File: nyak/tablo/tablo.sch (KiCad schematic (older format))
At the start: 109 parts

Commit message: more wiring
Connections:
- net Earth: now also U?.4 (E1), U?.4 (E1), U?.5 (E2), U?.5 (E2), U?.8 (GND), U?.8 (GND), U?.9 (GND), UOD1.7 (GND), UOD2.7 (GND)
- net GPIO12: now reaches U?.11 (Load)
- net GPIO12: now also JRPI.32 (Pin_32)
- net C1: now reaches U?.2 (D0)
- net C1: now also JRPI.7 (Pin_7), U?.2 (D0), U?.2 (D0), U?.2 (D0), U?.2 (D0), U?.2 (D0)
- net VCC: now reaches U?.20 (VCC)
- net VCC: now also U?.16 (VCC), U?.16 (VCC), U?.20 (VCC), U?.20 (VCC), U?.20 (VCC), U?.20 (VCC), U?.20 (VCC), UOD1.14 (VCC), UOD2.14 (VCC)
- net C2: now reaches U?.3 (D1)
- net C2: now also JRPI.29 (Pin_29), U?.3 (D1), U?.3 (D1), U?.3 (D1), U?.3 (D1), U?.3 (D1)
- net C3: now reaches U?.4 (D2)
- net C3: now also JRPI.31 (Pin_31), U?.4 (D2), U?.4 (D2), U?.4 (D2), U?.4 (D2), U?.4 (D2)
- net C4: now reaches U?.5 (D3)
- net C4: now also JRPI.26 (Pin_26), U?.5 (D3), U?.5 (D3), U?.5 (D3), U?.5 (D3), U?.5 (D3)
- net C5: now reaches U?.6 (D4)
- net C5: now also JRPI.24 (Pin_24), U?.6 (D4), U?.6 (D4), U?.6 (D4), U?.6 (D4), U?.6 (D4)
- net C6: now reaches U?.7 (D5)
- net C6: now also JRPI.21 (Pin_21), U?.7 (D5), U?.7 (D5), U?.7 (D5), U?.7 (D5), U?.7 (D5)
- net C7: now reaches U?.8 (D6)
- net C7: now also JRPI.19 (Pin_19), U?.8 (D6), U?.8 (D6), U?.8 (D6), U?.8 (D6), U?.8 (D6)
- net C8: now reaches U?.9 (D7)
- net C8: now also JRPI.23 (Pin_23), U?.9 (D7), U?.9 (D7), U?.9 (D7), U?.9 (D7), U?.9 (D7)
- net GPIO13: now reaches U?.11 (Load)
- net GPIO13: now also JRPI.33 (Pin_33)
- net GPIO14: now reaches U?.11 (Load)
- net GPIO14: now also JRPI.8 (Pin_8)
- net GPIO15: now reaches U?.11 (Load)
- net GPIO15: now also JRPI.10 (Pin_10)
- net GPIO16: now reaches U?.11 (Load)
- net GPIO16: now also JRPI.36 (Pin_36)
- net GPIO17: now reaches U?.11 (Load)
- net GPIO17: now also JRPI.11 (Pin_11)
- net AR1: now reaches U?.1 (A0)
- net AR1: now also JRPI.12 (Pin_12), U?.1 (A0)
- net AR2: now reaches U?.2 (A1)
- net AR2: now also JRPI.35 (Pin_35), U?.2 (A1)
- net AR3: now reaches U?.3 (A2)
- net AR3: now also JRPI.38 (Pin_38), U?.3 (A2)
- net GPIO22: now reaches U?.6 (E3)
- net GPIO22: now also JRPI.15 (Pin_15)
- net GPIO21: now reaches U?.6 (E3)
- net GPIO21: now also JRPI.40 (Pin_40)

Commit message: footprints added
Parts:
- JC1: footprint (none) -> Connector_PinHeader_2.54mm:PinHeader_1x08_P2.54mm_Vertical
- JC2, JC3, JC4, JC5, JC6, JR1, JR2: renamed from JC?; footprint (none) -> Connector_PinHeader_2.54mm:PinHeader_1x08_P2.54mm_Vertical
- JRPI1: renamed from JRPI; footprint (none) -> Connector_PinSocket_2.54mm:PinSocket_2x20_P2.54mm_Vertical
- QR1, QR10, QR11, QR12, QR2, QR3, QR4, QR5, QR6, QR7, QR8, QR9: renamed from Q?; footprint (none) -> Package_TO_SOT_THT:TO-220-3_Vertical
- RC1, RC10, RC11, RC12, RC13, RC14, RC15, RC16, RC17, RC18, RC19, RC2, RC20, RC21, RC22, RC23, RC24, RC25, RC26, RC27, RC28, RC29, RC3, RC30, RC31, RC32, RC33, RC34, RC35, RC36, RC37, RC38, RC39, RC4, RC40, RC41, RC42, RC43, RC44, RC45, RC46, RC47, RC48, RC5, RC6, RC7, RC8, RC9, RRB1, RRB10, RRB11, RRB12, RRB2, RRB3, RRB4, RRB5, RRB6, RRB7, RRB8, RRB9, RRE1, RRE10, RRE11, RRE12, RRE2, RRE3, RRE4, RRE5, RRE6, RRE7, RRE8, RRE9: renamed from R?; footprint (none) -> Resistor_THT:R_Axial_DIN0204_L3.6mm_D1.6mm_P7.62mm_Horizontal
- UC1, UC2, UC3, UC4, UC5, UC6: renamed from U?; footprint (none) -> Package_DIP:DIP-18_W7.62mm
- UDM1, UDM2: renamed from U?; footprint (none) -> Package_DIP:DIP-16_W7.62mm
- UL1, UL2, UL3, UL4, UL5, UL6: renamed from U?; footprint (none) -> Package_DIP:DIP-20_W7.62mm
- UOD1, UOD2: footprint (none) -> Package_DIP:DIP-14_W7.62mm
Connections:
- net Earth: now also QR1.3 (E), QR10.3 (E), QR11.3 (E), QR12.3 (E), QR2.3 (E), QR3.3 (E), QR4.3 (E), QR5.3 (E), QR6.3 (E), QR7.3 (E), QR8.3 (E), QR9.3 (E), RRE1.1, RRE10.1, RRE11.1, RRE12.1, RRE2.1, RRE3.1, RRE4.1, RRE5.1, RRE6.1, RRE7.1, RRE8.1, RRE9.1
- net at UL1.1 (OE): now also JRPI1.16 (Pin_16), UL2.1 (OE), UL3.1 (OE), UL4.1 (OE), UL5.1 (OE), UL6.1 (OE)

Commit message: more tracks
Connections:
- net at QR7.1 (B), RRE7.2: now also RRB7.2; no longer RRB8.2
- net at QR8.1 (B), RRE8.2: now also RRB8.2; no longer RRB7.2
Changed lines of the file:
@@
 	550  2200 550  2150
 Wire Wire Line
-	3300 2600 3300 1850
-Wire Wire Line
-	3300 1850 3000 1850
-Wire Wire Line
 	3000 1850 3000 1900
-Connection ~ 3000 1850
 Wire Wire Line
 	3000 1850 2800 1850
@@
 	3300 2700 3250 2700
 Wire Wire Line
-	3250 2700 3250 1800
-Wire Wire Line
-	3250 1800 2550 1800
-Wire Wire Line
 	2350 1800 2350 1850
 Wire Wire Line
 	2550 1800 2550 1900
-Connection ~ 2550 1800
 Wire Wire Line
 	2550 1800 2350 1800
@@
 Wire Wire Line
 	2900 3900 2900 3700
-Wire Bus Line
-	7700 1100 7700 10400
 Connection ~ 2450 4000
 Connection ~ 2900 3700
@@
 Wire Wire Line
 	650  2600 1000 2600
+Wire Wire Line
+	3300 2600 3300 1800
+Wire Wire Line
+	3300 1800 2550 1800
+Connection ~ 2550 1800
+Wire Wire Line
+	3250 2700 3250 1850
+Wire Wire Line
+	3250 1850 3000 1850
+Wire Bus Line
+	7700 1100 7700 10400
+Connection ~ 3000 1850
 $EndSCHEMATC

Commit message: more pcb
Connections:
- net Earth: now also UL1.10 (GND)
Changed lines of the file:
@@
 EESchema Schematic File Version 4
-LIBS:tablo-cache
-EELAYER 26 0
+EELAYER 30 0
 EELAYER END
 $Descr A3 16535 11693
@@
 	8950 10300 9100 10300
 Wire Wire Line
-	8450 2250 9500 2250
-Wire Wire Line
 	9500 2250 9500 1950
-Wire Wire Line
-	8450 4000 9500 4000
-Wire Wire Line
-	9500 4000 9500 3650
 Wire Wire Line
 	8450 5700 9500 5700
@@
 Wire Wire Line
 	9700 3650 9500 3650
-Connection ~ 9500 3650
 Wire Wire Line
 	9500 3650 9500 3600
@@
 Wire Wire Line
 	3250 1850 3000 1850
+Connection ~ 3000 1850
+Connection ~ 9500 3650
+Wire Wire Line
+	9500 4000 9500 3650
+Wire Wire Line
+	8450 4000 9500 4000
+Wire Wire Line
+	9500 2250 8450 2250
+Wire Wire Line
+	8450 2250 8450 2300
 Wire Bus Line
 	7700 1100 7700 10400
-Connection ~ 3000 1850
 $EndSCHEMATC

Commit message: seems to be finished
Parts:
- added JTAP1: Conn_01x02_Male, Connector_PinHeader_2.54mm:PinHeader_1x02_P2.54mm_Vertical, symbol Connector:Conn_01x02_Male
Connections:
- net Earth: now also JRPI1.6 (Pin_6), JTAP1.2 (Pin_2)
- net VCC: now also JRPI1.2 (Pin_2), JTAP1.1 (Pin_1)
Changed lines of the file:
@@
 Wire Wire Line
 	8450 2250 8450 2300
+$Comp
+L Connector:Conn_01x02_Male JTAP1
+U 1 1 5DEAD8D0
+P 5400 7700
+F 0 "JTAP1" H 5508 7881 50  0000 C CNN
+F 1 "Conn_01x02_Male" H 5508 7790 50  0000 C CNN
+F 2 "Connector_PinHeader_2.54mm:PinHeader_1x02_P2.54mm_Vertical" H 5400 7700 50  0001 C CNN
+F 3 "~" H 5400 7700 50  0001 C CNN
+	1    5400 7700
+	1    0    0    -1
+$EndComp
+$Comp
+L power:Earth #PWR0121
+U 1 1 5DEADD9C
+P 5900 7900
+F 0 "#PWR0121" H 5900 7650 50  0001 C CNN
+F 1 "Earth" H 5900 7750 50  0001 C CNN
+F 2 "" H 5900 7900 50  0001 C CNN
+F 3 "~" H 5900 7900 50  0001 C CNN
+	1    5900 7900
+	1    0    0    -1
+$EndComp
+Wire Wire Line
+	5900 7900 5900 7800
+Wire Wire Line
+	5900 7800 5600 7800
+$Comp
+L power:VCC #PWR0122
+U 1 1 5DF5E14E
+P 5900 7600
+F 0 "#PWR0122" H 5900 7450 50  0001 C CNN
+F 1 "VCC" H 5917 7773 50  0000 C CNN
+F 2 "" H 5900 7600 50  0001 C CNN
+F 3 "" H 5900 7600 50  0001 C CNN
+	1    5900 7600
+	1    0    0    -1
+$EndComp
+Wire Wire Line
+	5600 7700 5900 7700
+Wire Wire Line
+	5900 7700 5900 7600
+$Comp
+L power:VCC #PWR0123
+U 1 1 5DFB5291
+P 6050 4600
+F 0 "#PWR0123" H 6050 4450 50  0001 C CNN
+F 1 "VCC" H 6067 4773 50  0000 C CNN
+F 2 "" H 6050 4600 50  0001 C CNN
+F 3 "" H 6050 4600 50  0001 C CNN
+	1    6050 4600
+	1    0    0    -1
+$EndComp
+Wire Wire Line
+	5850 4650 6050 4650
+Wire Wire Line
+	6050 4650 6050 4600
+$Comp
+L power:Earth #PWR0124
+U 1 1 5E00CD77
+P 6000 4750
+F 0 "#PWR0124" H 6000 4500 50  0001 C CNN
+F 1 "Earth" H 6000 4600 50  0001 C CNN
+F 2 "" H 6000 4750 50  0001 C CNN
+F 3 "~" H 6000 4750 50  0001 C CNN
+	1    6000 4750
+	-1   0    0    1
+$EndComp
+Wire Wire Line
+	5850 4850 6000 4850
+Wire Wire Line
+	6000 4850 6000 4750
 Wire Bus Line
 	7700 1100 7700 10400

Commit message: updated rpi gpio connector footprint
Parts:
- JRPI1: footprint Connector_PinSocket_2.54mm:PinSocket_2x20_P2.54mm_Vertical -> Connector_PinHeader_2.54mm:PinHeader_2x20_P2.54mm_Vertical
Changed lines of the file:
@@
 EESchema Schematic File Version 4
+LIBS:tablo-cache
 EELAYER 30 0
 EELAYER END
@@
 F 0 "JRPI1" H 5600 6667 50  0000 C CNN
 F 1 "Conn_02x20_Odd_Even" H 5600 6576 50  0000 C CNN
-F 2 "Connector_PinSocket_2.54mm:PinSocket_2x20_P2.54mm_Vertical" H 5550 5550 50  0001 C CNN
+F 2 "Connector_PinHeader_2.54mm:PinHeader_2x20_P2.54mm_Vertical" H 5550 5550 50  0001 C CNN
 F 3 "~" H 5550 5550 50  0001 C CNN
 	1    5550 5550

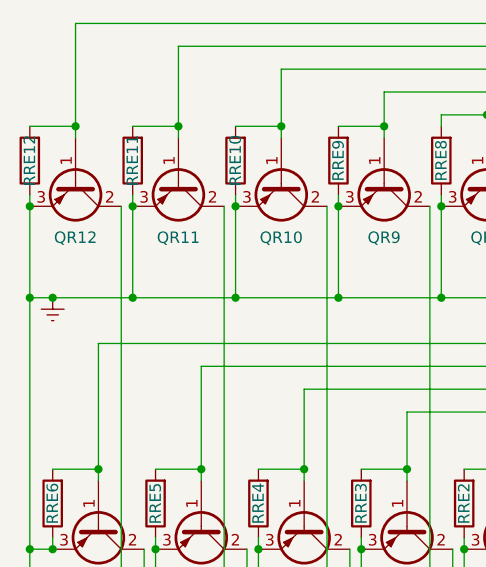
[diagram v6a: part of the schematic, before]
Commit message: Fixed row switch PNP transistor emitter connection from GND to VCC
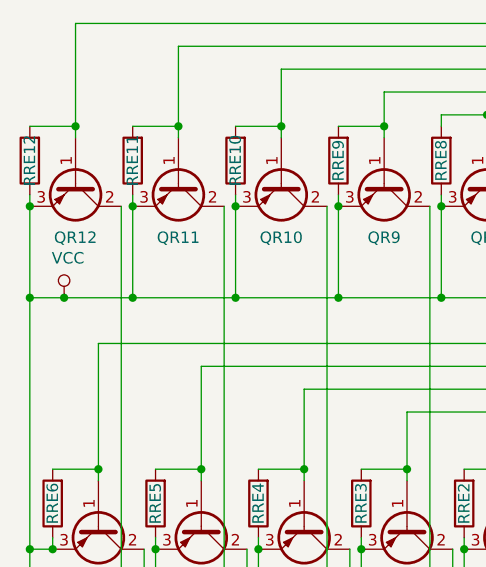
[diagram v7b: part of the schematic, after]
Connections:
- net Earth: no longer QR1.3 (E), QR10.3 (E), QR11.3 (E), QR12.3 (E), QR2.3 (E), QR3.3 (E), QR4.3 (E), QR5.3 (E), QR6.3 (E), QR7.3 (E), QR8.3 (E), QR9.3 (E), RRE1.1, RRE10.1, RRE11.1, RRE12.1, RRE2.1, RRE3.1, RRE4.1, RRE5.1, RRE6.1, RRE7.1, RRE8.1, RRE9.1
- net VCC: now also QR1.3 (E), QR10.3 (E), QR11.3 (E), QR12.3 (E), QR2.3 (E), QR3.3 (E), QR4.3 (E), QR5.3 (E), QR6.3 (E), QR7.3 (E), QR8.3 (E), QR9.3 (E), RRE1.1, RRE10.1, RRE11.1, RRE12.1, RRE2.1, RRE3.1, RRE4.1, RRE5.1, RRE6.1, RRE7.1, RRE8.1, RRE9.1
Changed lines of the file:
@@
 EESchema Schematic File Version 4
-LIBS:tablo-cache
 EELAYER 30 0
 EELAYER END
@@
 Title ""
 Date ""
-Rev ""
+Rev "1.1"
 Comp ""
 Comment1 ""
@@
 	550  2200 550  2600
 Wire Wire Line
-	550  2600 650  2600
-Wire Wire Line
 	1000 2600 1000 2200
 Connection ~ 550  2200
@@
 Connection ~ 2450 4000
 Connection ~ 2900 3700
-$Comp
-L power:Earth #PWR0120
-U 1 1 5F6E748E
-P 650 2600
-F 0 "#PWR0120" H 650 2350 50  0001 C CNN
-F 1 "Earth" H 650 2450 50  0001 C CNN
-F 2 "" H 650 2600 50  0001 C CNN
-F 3 "~" H 650 2600 50  0001 C CNN
-	1    650  2600
-	1    0    0    -1
-$EndComp
-Connection ~ 650  2600
-Wire Wire Line
-	650  2600 1000 2600
 Wire Wire Line
 	3300 2600 3300 1800
@@
 Wire Bus Line
 	7700 1100 7700 10400
+Wire Wire Line
+	550  2600 700  2600
+$Comp
+L power:VCC #PWR0120
+U 1 1 5E138797
+P 700 2600
+F 0 "#PWR0120" H 700 2450 50  0001 C CNN
+F 1 "VCC" H 717 2773 50  0000 C CNN
+F 2 "" H 700 2600 50  0001 C CNN
+F 3 "" H 700 2600 50  0001 C CNN
+	1    700  2600
+	1    0    0    -1
+$EndComp
+Connection ~ 700  2600
+Wire Wire Line
+	700  2600 1000 2600
 $EndSCHEMATC

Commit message: Updated resistor footprints to have 0.8mm holes instead of 0.7
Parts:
- RC1, RC10, RC11, RC12, RC13, RC14, RC15, RC16, RC17, RC18, RC19, RC2, RC20, RC21, RC22, RC23, RC24, RC25, RC26, RC27, RC28, RC29, RC3, RC30, RC31, RC32, RC33, RC34, RC35, RC36, RC37, RC38, RC39, RC4, RC40, RC41, RC42, RC43, RC44, RC45, RC46, RC47, RC48, RC5, RC6, RC7, RC8, RC9, RRB1, RRB10, RRB11, RRB12, RRB2, RRB3, RRB4, RRB5, RRB6, RRB7, RRB8, RRB9, RRE1, RRE10, RRE11, RRE12, RRE2, RRE3, RRE4, RRE5, RRE6, RRE7, RRE8, RRE9: footprint Resistor_THT:R_Axial_DIN0204_L3.6mm_D1.6mm_P7.62mm_Horizontal -> Resistor_THT:R_Axial_DIN0207_L6.3mm_D2.5mm_P7.62mm_Horizontal
